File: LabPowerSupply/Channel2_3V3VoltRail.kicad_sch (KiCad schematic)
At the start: 3 parts

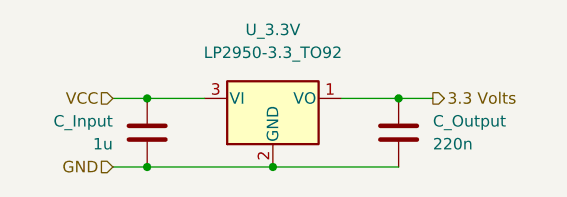
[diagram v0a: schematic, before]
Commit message: Finished first pass on the schematic
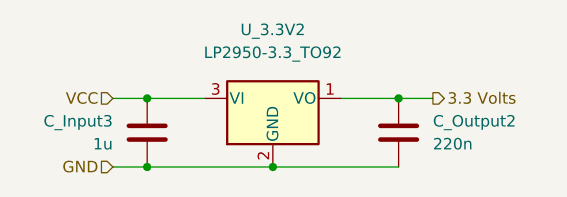
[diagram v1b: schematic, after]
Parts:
- renumbered C_Input to C_Input3, C_Output to C_Output2, U_3.3V to U_3.3V2
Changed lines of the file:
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@@
   (symbol (lib_id "Device:C") (at 127 105.41 0) (mirror x) (unit 1)
     (in_bom yes) (on_board yes) (fields_autoplaced)
-    (property "Reference" "C_Input" (id 0) (at 123.19 104.1399 0)
+    (property "Reference" "C_Input3" (id 0) (at 123.19 104.1399 0)
       (effects (font (size 1.27 1.27)) (justify right))
     )
@@
   (symbol (lib_id "Regulator_Linear:LP2950-3.3_TO92") (at 140.97 101.6 0) (unit 1)
     (in_bom yes) (on_board yes) (fields_autoplaced)
-    (property "Reference" "U_3.3V" (id 0) (at 140.97 93.98 0))
+    (property "Reference" "U_3.3V2" (id 0) (at 140.97 93.98 0))
     (property "Value" "LP2950-3.3_TO92" (id 1) (at 140.97 96.52 0))
     (property "Footprint" "Package_TO_SOT_THT:TO-92_Inline" (id 2) (at 140.97 95.885 0)
@@
   (symbol (lib_id "Device:C") (at 154.94 105.41 0) (unit 1)
     (in_bom yes) (on_board yes) (fields_autoplaced)
-    (property "Reference" "C_Output" (id 0) (at 158.75 104.1399 0)
+    (property "Reference" "C_Output2" (id 0) (at 158.75 104.1399 0)
       (effects (font (size 1.27 1.27)) (justify left))
     )

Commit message: started PCB
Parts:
- renumbered C_Input3 to C_Input2, U_3.3V2 to U_3.3V1
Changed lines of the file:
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@@
     (rev "1")
     (company "George Mason University")
-    (comment 3 "peripherals for use by the second channel microcontroller.")
+    (comment 1 "drawn by the digital system should reduce power losses.")
+    (comment 2 "voltage is VCC for the secondary side however the limited current")
+    (comment 3 "peripherals for use by and for the secondary MCU. The input")
     (comment 4 "This the linear voltage regulator use for powering the digital")
   )
@@
   (symbol (lib_id "Device:C") (at 127 105.41 0) (mirror x) (unit 1)
     (in_bom yes) (on_board yes) (fields_autoplaced)
-    (property "Reference" "C_Input3" (id 0) (at 123.19 104.1399 0)
+    (property "Reference" "C_Input2" (id 0) (at 123.19 104.1399 0)
       (effects (font (size 1.27 1.27)) (justify right))
     )
@@
   (symbol (lib_id "Regulator_Linear:LP2950-3.3_TO92") (at 140.97 101.6 0) (unit 1)
     (in_bom yes) (on_board yes) (fields_autoplaced)
-    (property "Reference" "U_3.3V2" (id 0) (at 140.97 93.98 0))
+    (property "Reference" "U_3.3V1" (id 0) (at 140.97 93.98 0))
     (property "Value" "LP2950-3.3_TO92" (id 1) (at 140.97 96.52 0))
     (property "Footprint" "Package_TO_SOT_THT:TO-92_Inline" (id 2) (at 140.97 95.885 0)

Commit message: more work
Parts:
- renumbered C_Input2 to C1_3.3V2, C_Output2 to C2_3.3V2, U_3.3V1 to U_3.3V2
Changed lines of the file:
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@@
   (symbol (lib_id "Device:C") (at 127 105.41 0) (mirror x) (unit 1)
     (in_bom yes) (on_board yes) (fields_autoplaced)
-    (property "Reference" "C_Input2" (id 0) (at 123.19 104.1399 0)
+    (property "Reference" "C1_3.3V2" (id 0) (at 123.19 104.1399 0)
       (effects (font (size 1.27 1.27)) (justify right))
     )
@@
   (symbol (lib_id "Regulator_Linear:LP2950-3.3_TO92") (at 140.97 101.6 0) (unit 1)
     (in_bom yes) (on_board yes) (fields_autoplaced)
-    (property "Reference" "U_3.3V1" (id 0) (at 140.97 93.98 0))
+    (property "Reference" "U_3.3V2" (id 0) (at 140.97 93.98 0))
     (property "Value" "LP2950-3.3_TO92" (id 1) (at 140.97 96.52 0))
     (property "Footprint" "Package_TO_SOT_THT:TO-92_Inline" (id 2) (at 140.97 95.885 0)
@@
   (symbol (lib_id "Device:C") (at 154.94 105.41 0) (unit 1)
     (in_bom yes) (on_board yes) (fields_autoplaced)
-    (property "Reference" "C_Output2" (id 0) (at 158.75 104.1399 0)
+    (property "Reference" "C2_3.3V2" (id 0) (at 158.75 104.1399 0)
       (effects (font (size 1.27 1.27)) (justify left))
     )

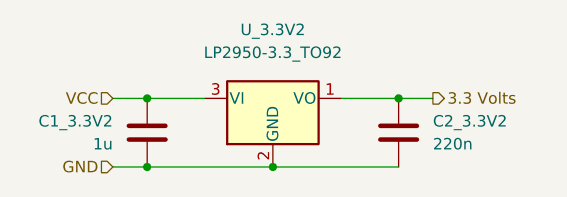
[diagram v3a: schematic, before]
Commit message: Resistor footprints changed to 0603
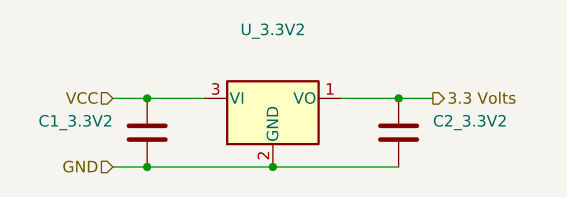
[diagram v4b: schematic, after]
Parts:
- C1_3.3V2: value 1u -> (none); footprint Capacitor_SMD:C_1210_3225Metric -> (none)
- C2_3.3V2: value 220n -> (none); footprint Capacitor_SMD:C_1210_3225Metric -> (none)
- U_3.3V2: value LP2950-3.3_TO92 -> (none); footprint Package_TO_SOT_THT:TO-92_Inline -> (none)
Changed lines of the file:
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@@
       (effects (font (size 1.27 1.27)) (justify right))
     )
-    (property "Value" "1u" (id 1) (at 123.19 106.6799 0)
+    (property "Value" "" (id 1) (at 123.19 106.6799 0)
       (effects (font (size 1.27 1.27)) (justify right))
     )
-    (property "Footprint" "Capacitor_SMD:C_1210_3225Metric" (id 2) (at 127.9652 101.6 0)
+    (property "Footprint" "" (id 2) (at 127.9652 101.6 0)
       (effects (font (size 1.27 1.27)) hide)
     )
@@
     (in_bom yes) (on_board yes) (fields_autoplaced)
     (property "Reference" "U_3.3V2" (id 0) (at 140.97 93.98 0))
-    (property "Value" "LP2950-3.3_TO92" (id 1) (at 140.97 96.52 0))
-    (property "Footprint" "Package_TO_SOT_THT:TO-92_Inline" (id 2) (at 140.97 95.885 0)
+    (property "Value" "" (id 1) (at 140.97 96.52 0))
+    (property "Footprint" "" (id 2) (at 140.97 95.885 0)
       (effects (font (size 1.27 1.27) italic) hide)
     )
@@
       (effects (font (size 1.27 1.27)) (justify left))
     )
-    (property "Value" "220n" (id 1) (at 158.75 106.6799 0)
+    (property "Value" "" (id 1) (at 158.75 106.6799 0)
       (effects (font (size 1.27 1.27)) (justify left))
     )
-    (property "Footprint" "Capacitor_SMD:C_1210_3225Metric" (id 2) (at 155.9052 109.22 0)
+    (property "Footprint" "" (id 2) (at 155.9052 109.22 0)
       (effects (font (size 1.27 1.27)) hide)
     )

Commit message: Added mcu capacitors, split 5v inductors
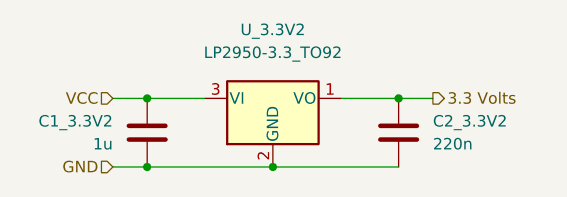
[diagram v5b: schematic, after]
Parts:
- C1_3.3V2: value (none) -> 1u; footprint (none) -> Capacitor_THT:C_Disc_D5.0mm_W2.5mm_P2.50mm
- C2_3.3V2: value (none) -> 220n; footprint (none) -> Capacitor_THT:C_Disc_D5.0mm_W2.5mm_P2.50mm
- U_3.3V2: value (none) -> LP2950-3.3_TO92; footprint (none) -> Package_TO_SOT_THT:TO-92_Inline
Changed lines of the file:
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@@
       (effects (font (size 1.27 1.27)) (justify right))
     )
-    (property "Value" "" (id 1) (at 123.19 106.6799 0)
+    (property "Value" "1u" (id 1) (at 123.19 106.6799 0)
       (effects (font (size 1.27 1.27)) (justify right))
     )
-    (property "Footprint" "" (id 2) (at 127.9652 101.6 0)
+    (property "Footprint" "Capacitor_THT:C_Disc_D5.0mm_W2.5mm_P2.50mm" (id 2) (at 127.9652 101.6 0)
       (effects (font (size 1.27 1.27)) hide)
     )
@@
     (in_bom yes) (on_board yes) (fields_autoplaced)
     (property "Reference" "U_3.3V2" (id 0) (at 140.97 93.98 0))
-    (property "Value" "" (id 1) (at 140.97 96.52 0))
-    (property "Footprint" "" (id 2) (at 140.97 95.885 0)
+    (property "Value" "LP2950-3.3_TO92" (id 1) (at 140.97 96.52 0))
+    (property "Footprint" "Package_TO_SOT_THT:TO-92_Inline" (id 2) (at 140.97 95.885 0)
       (effects (font (size 1.27 1.27) italic) hide)
     )
@@
       (effects (font (size 1.27 1.27)) (justify left))
     )
-    (property "Value" "" (id 1) (at 158.75 106.6799 0)
+    (property "Value" "220n" (id 1) (at 158.75 106.6799 0)
       (effects (font (size 1.27 1.27)) (justify left))
     )
-    (property "Footprint" "" (id 2) (at 155.9052 109.22 0)
+    (property "Footprint" "Capacitor_THT:C_Disc_D5.0mm_W2.5mm_P2.50mm" (id 2) (at 155.9052 109.22 0)
       (effects (font (size 1.27 1.27)) hide)
     )

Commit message: Fixed 5v/3v regulators, fixed switching regulator comp
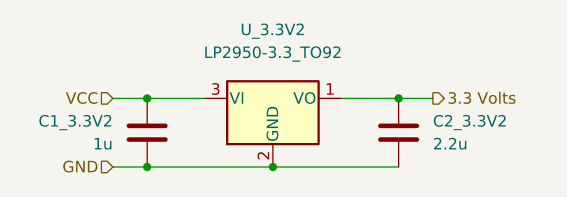
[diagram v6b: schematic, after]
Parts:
- C2_3.3V2: value 220n -> 2.2u
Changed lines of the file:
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@@
       (effects (font (size 1.27 1.27)) (justify left))
     )
-    (property "Value" "220n" (id 1) (at 158.75 106.6799 0)
+    (property "Value" "2.2u" (id 1) (at 158.75 106.6799 0)
       (effects (font (size 1.27 1.27)) (justify left))
     )

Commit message: Changed most parts to smd
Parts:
- C1_3.3V2, C2_3.3V2: footprint Capacitor_THT:C_Disc_D5.0mm_W2.5mm_P2.50mm -> Capacitor_SMD:C_0805_2012Metric
- U_3.3V2: footprint Package_TO_SOT_THT:TO-92_Inline -> Package_TO_SOT_SMD:TO-252-3_TabPin4
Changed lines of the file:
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@@
       (effects (font (size 1.27 1.27)) (justify right))
     )
-    (property "Footprint" "Capacitor_THT:C_Disc_D5.0mm_W2.5mm_P2.50mm" (id 2) (at 127.9652 101.6 0)
+    (property "Footprint" "Capacitor_SMD:C_0805_2012Metric" (id 2) (at 127.9652 101.6 0)
       (effects (font (size 1.27 1.27)) hide)
     )
@@
     (property "Reference" "U_3.3V2" (id 0) (at 140.97 93.98 0))
     (property "Value" "LP2950-3.3_TO92" (id 1) (at 140.97 96.52 0))
-    (property "Footprint" "Package_TO_SOT_THT:TO-92_Inline" (id 2) (at 140.97 95.885 0)
+    (property "Footprint" "Package_TO_SOT_SMD:TO-252-3_TabPin4" (id 2) (at 140.97 95.885 0)
       (effects (font (size 1.27 1.27) italic) hide)
     )
@@
       (effects (font (size 1.27 1.27)) (justify left))
     )
-    (property "Footprint" "Capacitor_THT:C_Disc_D5.0mm_W2.5mm_P2.50mm" (id 2) (at 155.9052 109.22 0)
+    (property "Footprint" "Capacitor_SMD:C_0805_2012Metric" (id 2) (at 155.9052 109.22 0)
       (effects (font (size 1.27 1.27)) hide)
     )

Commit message: almost done
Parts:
- C1_3.3V2: footprint Capacitor_SMD:C_0805_2012Metric -> Capacitor_SMD:C_0603_1608Metric
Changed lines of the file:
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@@
       (effects (font (size 1.27 1.27)) (justify right))
     )
-    (property "Footprint" "Capacitor_SMD:C_0805_2012Metric" (id 2) (at 127.9652 101.6 0)
+    (property "Footprint" "Capacitor_SMD:C_0603_1608Metric" (id 2) (at 127.9652 101.6 0)
       (effects (font (size 1.27 1.27)) hide)
     )
